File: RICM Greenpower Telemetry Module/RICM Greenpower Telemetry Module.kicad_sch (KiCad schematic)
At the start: 35 parts, among them J1 Conn_01x02_Female, J10 Conn_01x02_Female, J11 Conn_01x02_Female, J2 Conn_01x02_Female, J3 Conn_01x02_Female, J4 Jack-DC, J5 Conn_01x05_Female, J6 Conn_02x04_Counter_Clockwise, J7 Conn_01x03_Female, J8 Conn_01x03_Female, J9 Conn_01x04_Female, U1 Pico, U2 MPU_6050_module, U3 Adafruit_MicroSD_SPI_SDIO, U4 LTC2990

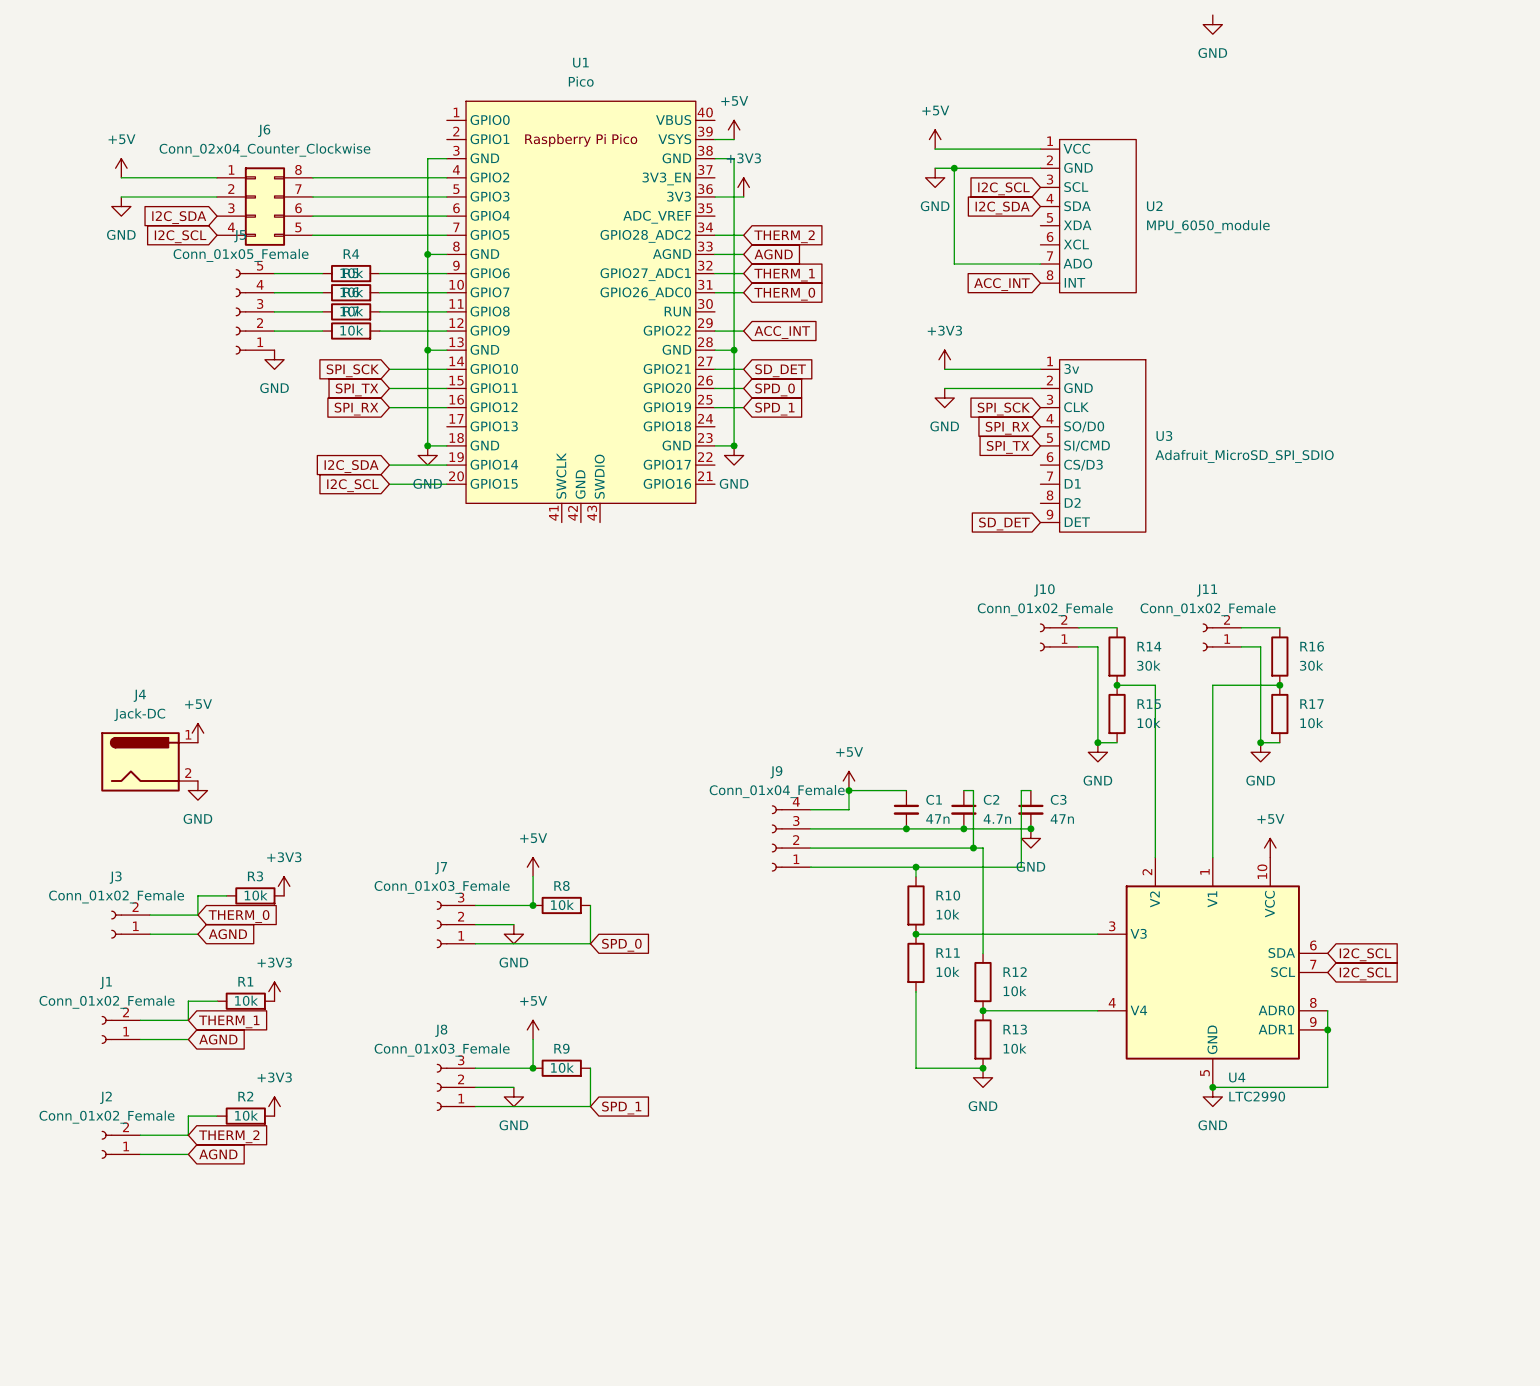
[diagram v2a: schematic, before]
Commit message: bug fixes and missing connections
Fixed the short from the first battery voltage to ground
Added a chip select for interfacing the SD card over SPI
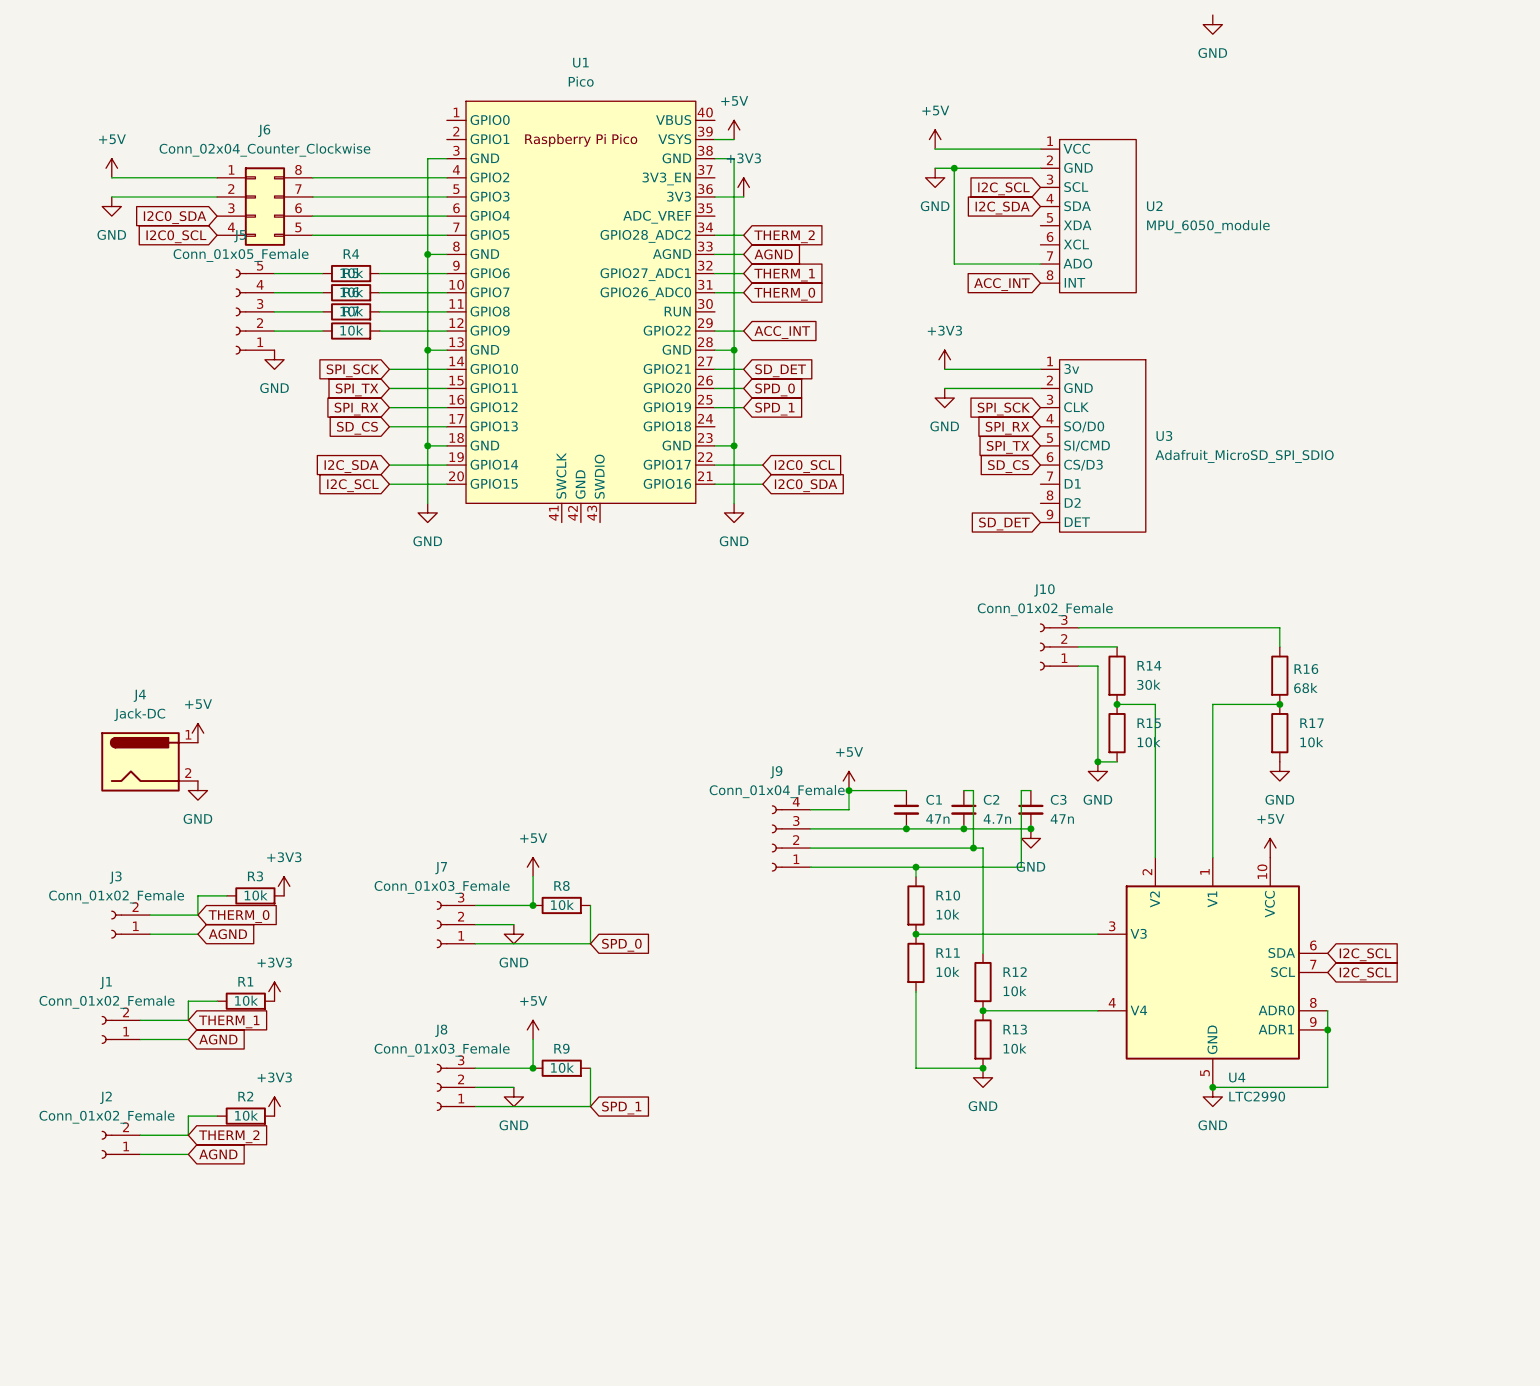
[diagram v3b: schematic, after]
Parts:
- removed J11: Conn_01x02_Female, Connector_PinHeader_2.54mm:PinHeader_1x02_P2.54mm_Vertical, symbol Connector:Conn_01x02_Female
- J10: symbol Connector:Conn_01x02_Female -> Connector:Conn_01x03_Female
- R16: value 30k -> 68k
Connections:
- net I2C_SCL: no longer J6.4 (Pin_4)
- net I2C_SDA: no longer J6.3 (Pin_3)
- net at R16.1: now also J10.3 (Pin_3)
- net SD_CS: now reaches U3.6 (CS/D3)
- net SD_CS: now also U1.17 (GPIO13)
- net I2C0_SDA: now reaches U1.21 (GPIO16)
- net I2C0_SDA: now also J6.3 (Pin_3)
- net I2C0_SCL: now reaches U1.22 (GPIO17)
- net I2C0_SCL: now also J6.4 (Pin_4)
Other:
- moved on the sheet: R14, R15, R16, R17

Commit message: first draft of layout
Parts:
- C1, C2, C3: footprint Capacitor_THT:C_Disc_D7.5mm_W5.0mm_P5.00mm -> Capacitor_THT:C_Disc_D4.7mm_W2.5mm_P5.00mm
- J10: footprint Connector_PinHeader_2.54mm:PinHeader_1x02_P2.54mm_Vertical -> Connector_PinHeader_2.54mm:PinHeader_1x03_P2.54mm_Vertical
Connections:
- net I2C0_SCL: now also U1.20 (GPIO15); no longer U1.22 (GPIO17)
- net I2C0_SDA: now also U1.19 (GPIO14); no longer U1.21 (GPIO16)
- net I2C_SCL: now also U1.22 (GPIO17); no longer U1.20 (GPIO15), U4.6 (SDA)
- net I2C_SDA: now also U1.21 (GPIO16), U4.6 (SDA); no longer U1.19 (GPIO14)

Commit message: Polyfuse and missing connections
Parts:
- added F1: Polyfuse, Capacitor_THT:C_Disc_D5.0mm_W2.5mm_P5.00mm, symbol Device:Polyfuse
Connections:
- net +5V: now also F1.2; no longer J4.1
- new net: F1.1, J4.1
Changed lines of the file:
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@@
+    (stroke (width 0) (type default) (color 0 0 0 0))
+  )
+  (wire (pts (xy 52.07 105.41) (xy 46.99 105.41))
     (stroke (width 0) (type default) (color 0 0 0 0))
   )
@@
   )
   (wire (pts (xy 134.62 26.67) (xy 148.59 26.67))
+    (stroke (width 0) (type default) (color 0 0 0 0))
+  )
+  (wire (pts (xy 39.37 105.41) (xy 36.83 105.41))
     (stroke (width 0) (type default) (color 0 0 0 0))
   )
@@
     (pin "2")
   )
+  (symbol (lib_id "Device:Polyfuse") (at 43.18 105.41 90) (unit 1)
+    (in_bom yes) (on_board yes) (fields_autoplaced)
+    (property "Reference" "F1" (id 0) (at 43.18 100.3132 90))
+    (property "Value" "Polyfuse" (id 1) (at 43.18 102.8501 90))
+    (property "Footprint" "Capacitor_THT:C_Disc_D5.0mm_W2.5mm_P5.00mm" (id 2) (at 48.26 104.14 0)
+      (effects (font (size 1.27 1.27)) (justify left) hide)
+    )
+    (property "Datasheet" "~" (id 3) (at 43.18 105.41 0)
+      (effects (font (size 1.27 1.27)) hide)
+    )
+    (pin "1")
+    (pin "2")
+  )
   (symbol (lib_id "Connector_Generic:Conn_02x04_Counter_Clockwise") (at 44.45 33.02 0) (unit 1)
     (in_bom yes) (on_board yes) (fields_autoplaced)
@@
     (pin "1")
   )
-  (symbol (lib_id "power:+5V") (at 36.83 105.41 0) (unit 1)
-    (in_bom yes) (on_board yes) (fields_autoplaced)
-    (property "Reference" "#PWR03" (id 0) (at 36.83 109.22 0)
-      (effects (font (size 1.27 1.27)) hide)
-    )
-    (property "Value" "+5V" (id 1) (at 36.83 100.33 0))
-    (property "Footprint" "" (id 2) (at 36.83 105.41 0)
-      (effects (font (size 1.27 1.27)) hide)
-    )
-    (property "Datasheet" "" (id 3) (at 36.83 105.41 0)
+  (symbol (lib_id "power:+5V") (at 52.07 105.41 0) (unit 1)
+    (in_bom yes) (on_board yes) (fields_autoplaced)
+    (property "Reference" "#PWR03" (id 0) (at 52.07 109.22 0)
+      (effects (font (size 1.27 1.27)) hide)
+    )
+    (property "Value" "+5V" (id 1) (at 52.07 100.33 0))
+    (property "Footprint" "" (id 2) (at 52.07 105.41 0)
+      (effects (font (size 1.27 1.27)) hide)
+    )
+    (property "Datasheet" "" (id 3) (at 52.07 105.41 0)
       (effects (font (size 1.27 1.27)) hide)
     )
@@
       (reference "C3") (unit 1) (value "47n") (footprint "Capacitor_THT:C_Disc_D4.7mm_W2.5mm_P5.00mm")
     )
+    (path "/5eb649d3-af57-43ba-a61a-b94807185dd7"
+      (reference "F1") (unit 1) (value "Polyfuse") (footprint "Capacitor_THT:C_Disc_D5.0mm_W2.5mm_P5.00mm")
+    )
     (path "/fdf3efc1-70d5-4d48-bbb6-43cffac36697"

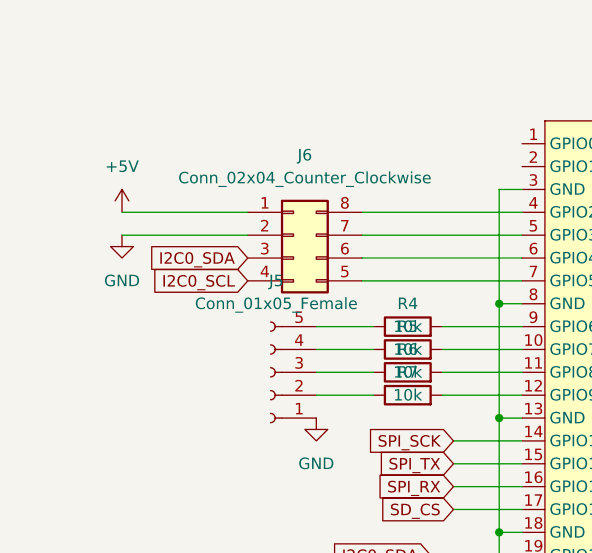
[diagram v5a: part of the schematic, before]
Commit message: update cluster
Updated cluster schematic to use an I2C gpio expander. Added two pushbutton switches.
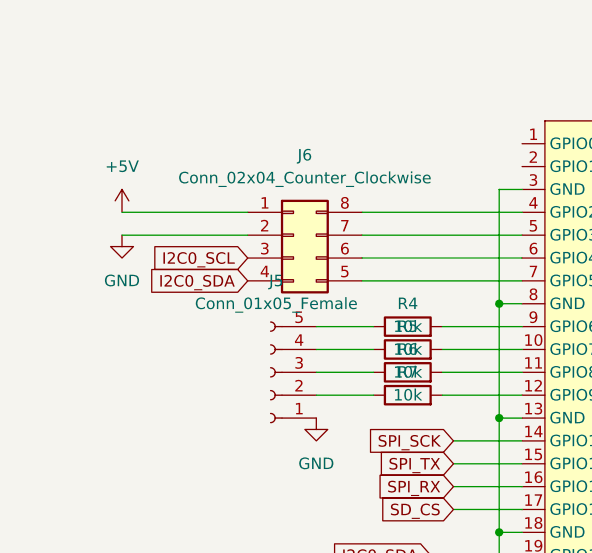
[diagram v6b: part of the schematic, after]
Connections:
- net I2C0_SCL: now also J6.3 (Pin_3); no longer J6.4 (Pin_4)
- net I2C0_SDA: now also J6.4 (Pin_4); no longer J6.3 (Pin_3)
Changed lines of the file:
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@@
     )
   )
-  (global_label "I2C0_SDA" (shape input) (at 39.37 35.56 180) (fields_autoplaced)
+  (global_label "I2C0_SDA" (shape input) (at 39.37 38.1 180) (fields_autoplaced)
     (effects (font (size 1.27 1.27)) (justify right))
-    (property "Intersheet References" "${INTERSHEET_REFS}" (id 0) (at 28.1274 35.6394 0)
+    (property "Intersheet References" "${INTERSHEET_REFS}" (id 0) (at 28.1274 38.1794 0)
       (effects (font (size 1.27 1.27)) (justify right) hide)
     )
@@
     )
   )
-  (global_label "I2C0_SCL" (shape input) (at 39.37 38.1 180) (fields_autoplaced)
+  (global_label "I2C0_SCL" (shape input) (at 39.37 35.56 180) (fields_autoplaced)
     (effects (font (size 1.27 1.27)) (justify right))
-    (property "Intersheet References" "${INTERSHEET_REFS}" (id 0) (at 28.1879 38.1794 0)
+    (property "Intersheet References" "${INTERSHEET_REFS}" (id 0) (at 28.1879 35.6394 0)
       (effects (font (size 1.27 1.27)) (justify right) hide)
     )
